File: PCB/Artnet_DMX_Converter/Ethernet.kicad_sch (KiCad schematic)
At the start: 90 parts, among them J3 RJ45, T1 FA2805, U4 W5500, U5 VO618A-3X019T, U6 SI3402-B-GMR, U7 TLV431, Y2 ABM8-25.000MHZ-10-D1G-T

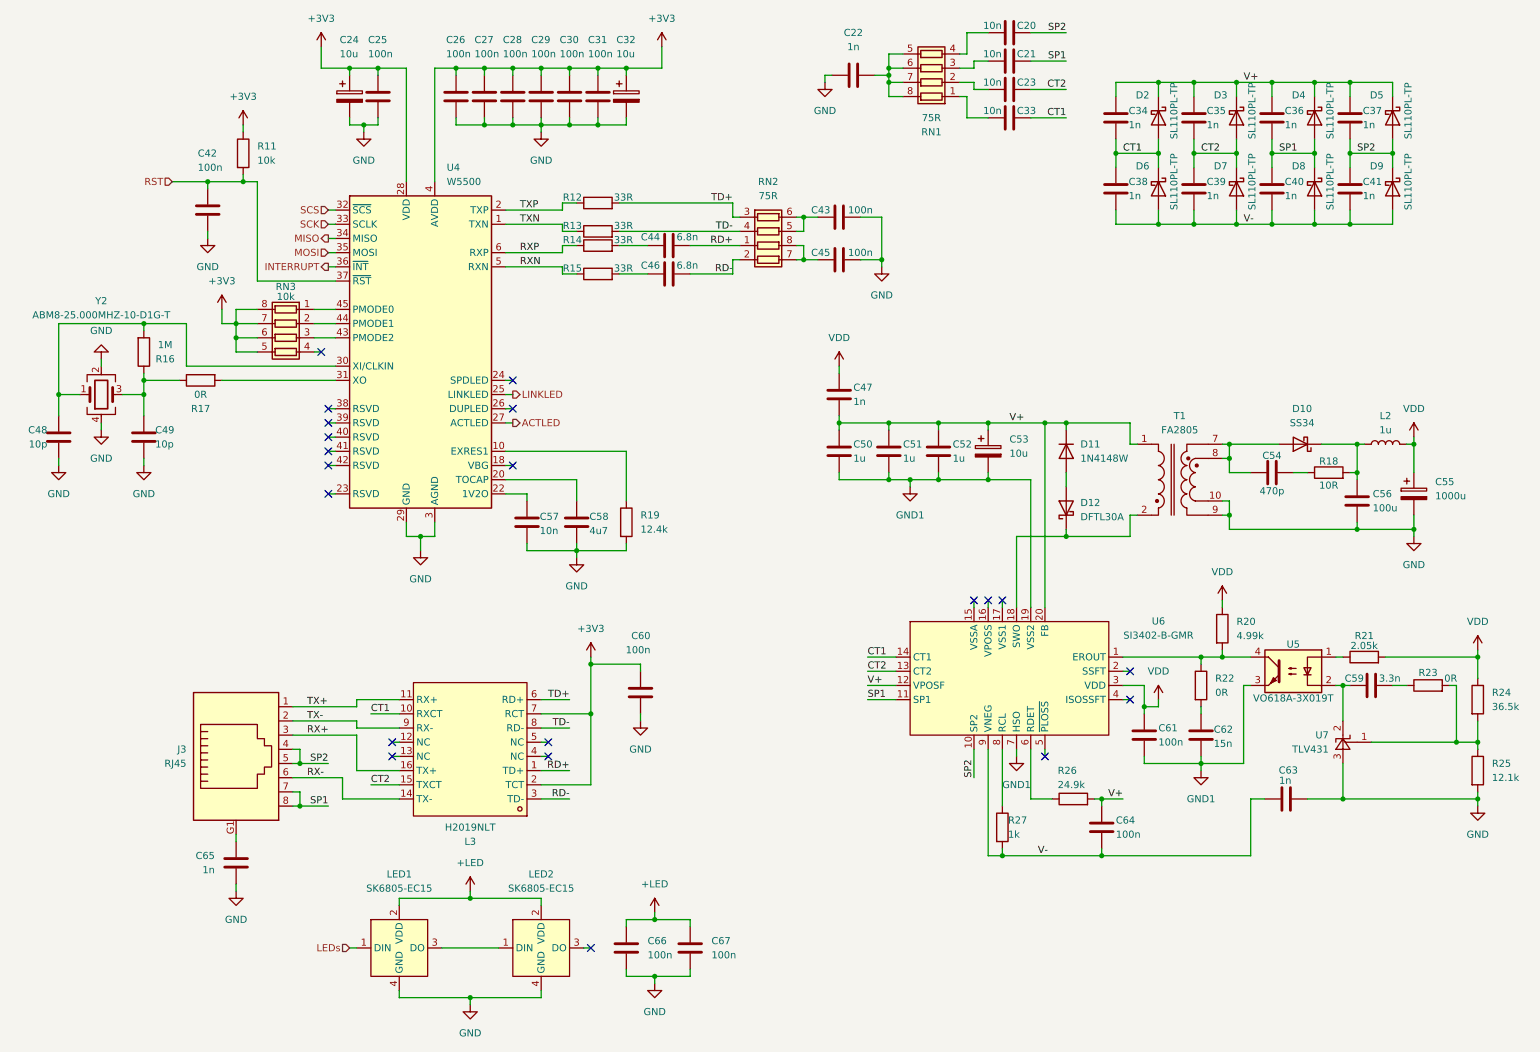
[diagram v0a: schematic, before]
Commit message: Updated the PCB Allot
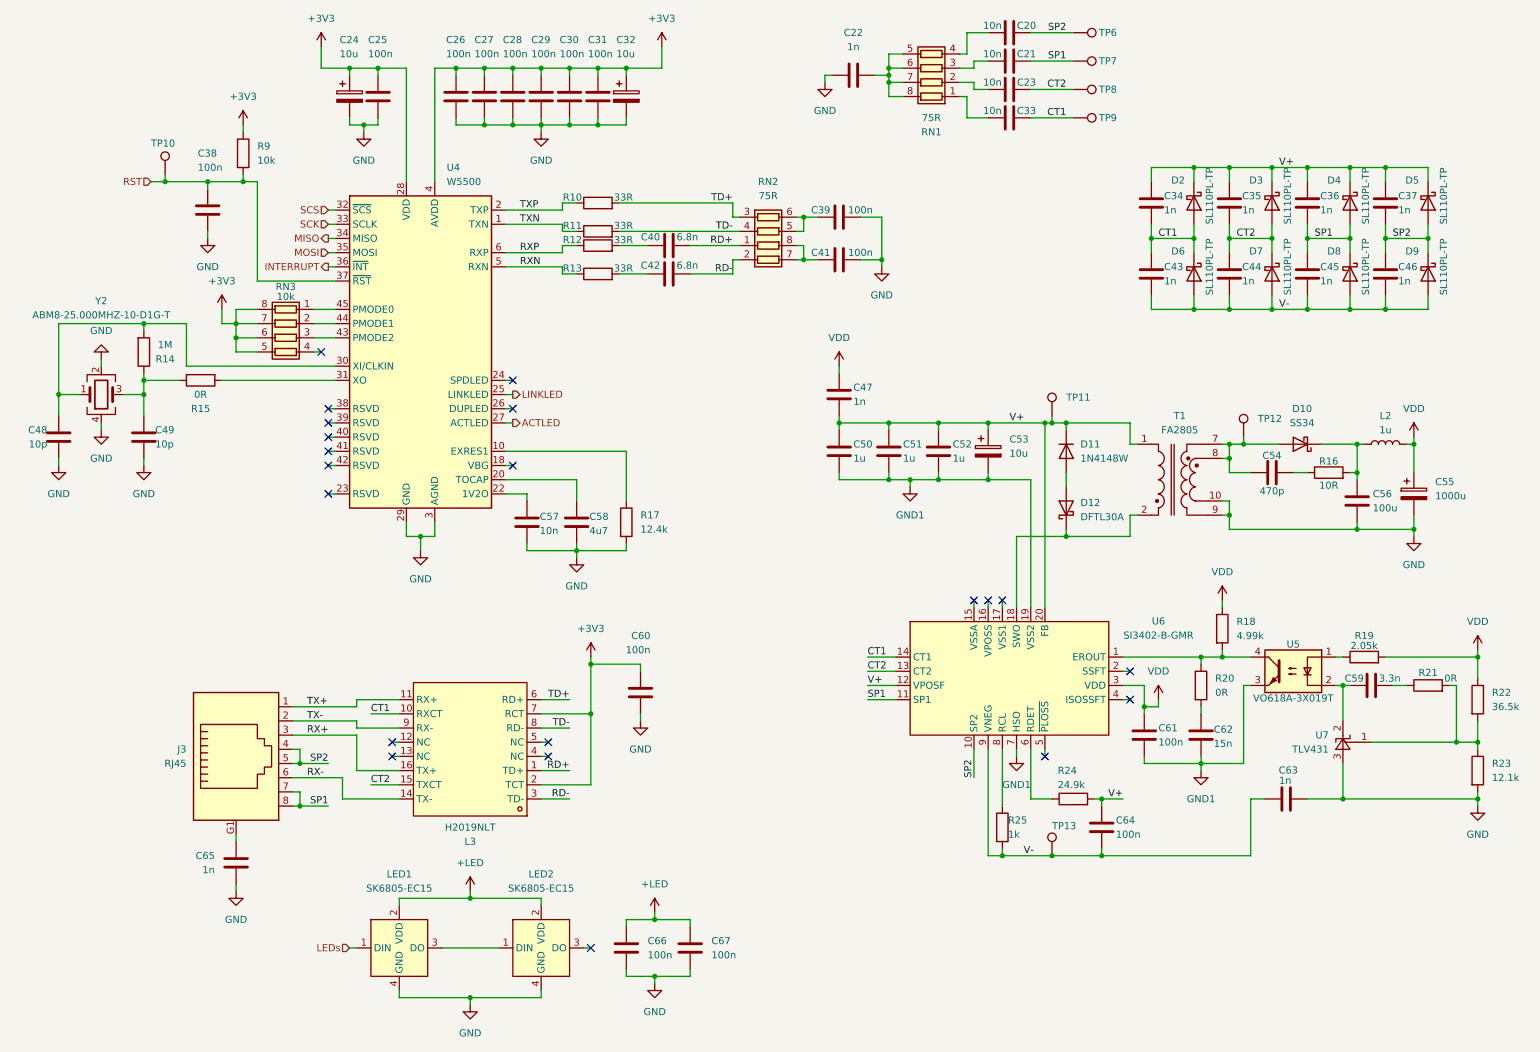
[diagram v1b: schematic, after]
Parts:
- added TP10, TP11, TP12, TP13, TP6, TP7, TP8, TP9: TestPoint, TestPoint:TestPoint_Pad_D1.5mm, symbol Connector:TestPoint
- renumbered C42 to C38, C43 to C39, C44 to C40, C45 to C41, C46 to C42, C38 to C43, C39 to C44, C40 to C45, C41 to C46, R12 to R10, R13 to R11, R14 to R12, R15 to R13, R16 to R14, R17 to R15, R18 to R16, R19 to R17, R20 to R18, R21 to R19, R22 to R20, R23 to R21, R24 to R22, R25 to R23, R26 to R24, R27 to R25, R11 to R9
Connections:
- net CT1: now also TP9.1
- net CT2: now also TP8.1
- net RST: now also TP10.1
- net SP1: now also TP7.1
- net SP2: now also TP6.1
- net V+: now also TP11.1
- net V-: now also TP13.1
- net at C54.1, D10.2 (A), T1.7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: now also TP12.1
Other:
- moved on the sheet: C34, C35, C36, C37, C43, C44, C45, C46, D2, D3, D4, D5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
